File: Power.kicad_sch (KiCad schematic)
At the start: 30 parts, among them J1 Jack-DC, J2 USB_B_Micro, J3 MCU_VOLTAGE_SEL, U1 LM2596S-5, U3 LM1117-3.3, U4 LM1117-1.8, U5 TPS2552DBVR

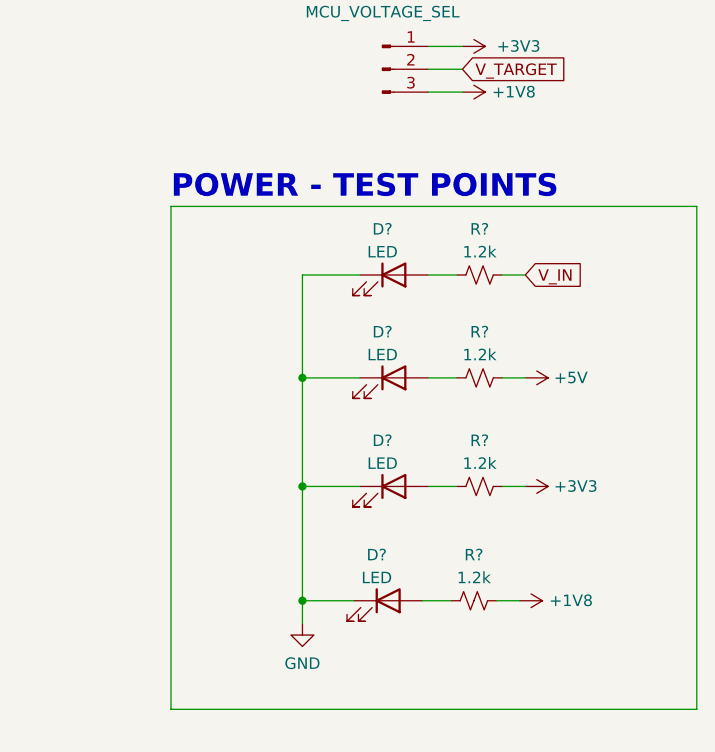
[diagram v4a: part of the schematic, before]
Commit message: Power ledler eklendi
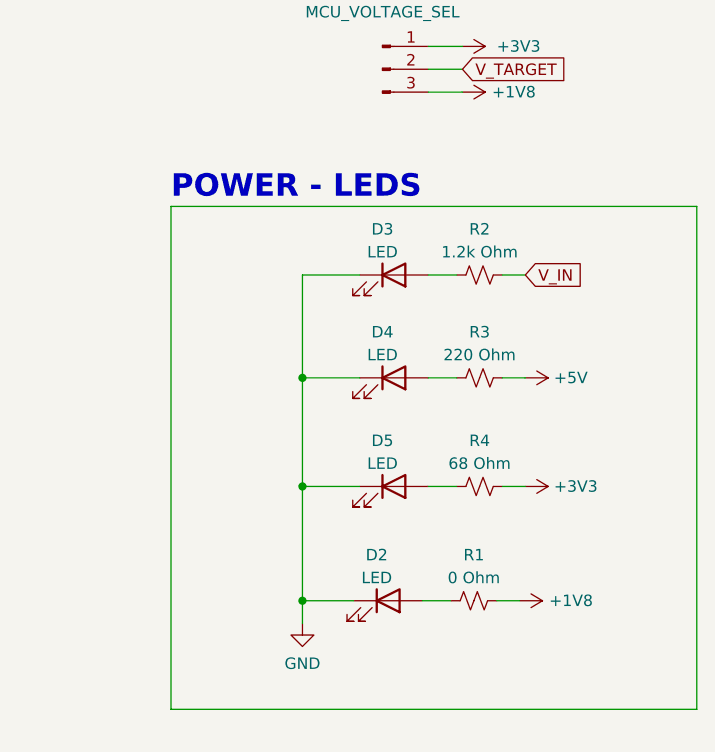
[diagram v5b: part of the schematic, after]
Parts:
- D2, D3, D4, D5: renamed from D?; footprint (none) -> LED_SMD:LED_0805_2012Metric
- R1: renamed from R?; value 1.2k -> 0 Ohm; footprint (none) -> Resistor_SMD:R_0603_1608Metric
- R2: renamed from R?; value 1.2k -> 1.2k Ohm; footprint (none) -> Resistor_SMD:R_0603_1608Metric
- R3: renamed from R?; value 1.2k -> 220 Ohm; footprint (none) -> Resistor_SMD:R_0603_1608Metric
- R4: renamed from R?; value 1.2k -> 68 Ohm; footprint (none) -> Resistor_SMD:R_0603_1608Metric
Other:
- note added: "POWER - LEDS"
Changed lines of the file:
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@@
     (effects (font (size 2.5 2.5) (thickness 0.5) bold) (justify left bottom))
   )
-  (text "POWER - TEST POINTS" (at 222.25 106.045 0)
+  (text "POWER - LEDS" (at 222.25 106.045 0)
     (effects (font (size 2.5 2.5) (thickness 0.5) bold) (justify left bottom))
   )
@@
   (symbol (lib_id "Device:R_Small_US") (at 255.905 150.495 90) (unit 1)
     (in_bom yes) (on_board yes)
-    (property "Reference" "R?" (id 0) (at 255.905 145.415 90))
-    (property "Value" "1.2k" (id 1) (at 255.905 147.955 90))
-    (property "Footprint" "" (id 2) (at 255.905 150.495 0)
+    (property "Reference" "R1" (id 0) (at 255.905 145.415 90))
+    (property "Value" "0 Ohm" (id 1) (at 255.905 147.955 90))
+    (property "Footprint" "Resistor_SMD:R_0603_1608Metric" (id 2) (at 255.905 150.495 0)
       (effects (font (size 1.27 1.27)) hide)
     )
@@
   (symbol (lib_id "Device:R_Small_US") (at 256.54 125.73 90) (unit 1)
     (in_bom yes) (on_board yes)
-    (property "Reference" "R?" (id 0) (at 256.54 120.65 90))
-    (property "Value" "1.2k" (id 1) (at 256.54 123.19 90))
-    (property "Footprint" "" (id 2) (at 256.54 125.73 0)
+    (property "Reference" "R3" (id 0) (at 256.54 120.65 90))
+    (property "Value" "220 Ohm" (id 1) (at 256.54 123.19 90))
+    (property "Footprint" "Resistor_SMD:R_0603_1608Metric" (id 2) (at 256.54 125.73 0)
       (effects (font (size 1.27 1.27)) hide)
     )
@@
   (symbol (lib_id "power:+1V8") (at 260.985 150.495 270) (unit 1)
     (in_bom yes) (on_board yes)
-    (property "Reference" "#PWR?" (id 0) (at 257.175 150.495 0)
+    (property "Reference" "#PWR0125" (id 0) (at 257.175 150.495 0)
       (effects (font (size 1.27 1.27)) hide)
     )
@@
   (symbol (lib_id "Device:R_Small_US") (at 256.54 137.795 90) (unit 1)
     (in_bom yes) (on_board yes)
-    (property "Reference" "R?" (id 0) (at 256.54 132.715 90))
-    (property "Value" "1.2k" (id 1) (at 256.54 135.255 90))
-    (property "Footprint" "" (id 2) (at 256.54 137.795 0)
+    (property "Reference" "R4" (id 0) (at 256.54 132.715 90))
+    (property "Value" "68 Ohm" (id 1) (at 256.54 135.255 90))
+    (property "Footprint" "Resistor_SMD:R_0603_1608Metric" (id 2) (at 256.54 137.795 0)
       (effects (font (size 1.27 1.27)) hide)
     )
@@
   (symbol (lib_name "LED_1") (lib_id "Device:LED") (at 246.38 150.495 0) (unit 1)
     (in_bom yes) (on_board yes)
-    (property "Reference" "D?" (id 0) (at 245.11 145.415 0))
+    (property "Reference" "D2" (id 0) (at 245.11 145.415 0))
     (property "Value" "LED" (id 1) (at 245.11 147.955 0))
-    (property "Footprint" "" (id 2) (at 246.38 150.495 0)
+    (property "Footprint" "LED_SMD:LED_0805_2012Metric" (id 2) (at 246.38 150.495 0)
       (effects (font (size 1.27 1.27)) hide)
     )
@@
   (symbol (lib_id "power:+3V3") (at 261.62 137.795 270) (unit 1)
     (in_bom yes) (on_board yes) (fields_autoplaced)
-    (property "Reference" "#PWR?" (id 0) (at 257.81 137.795 0)
+    (property "Reference" "#PWR0123" (id 0) (at 257.81 137.795 0)
       (effects (font (size 1.27 1.27)) hide)
     )
@@
   (symbol (lib_id "Device:R_Small_US") (at 256.54 114.3 90) (unit 1)
     (in_bom yes) (on_board yes)
-    (property "Reference" "R?" (id 0) (at 256.54 109.22 90))
-    (property "Value" "1.2k" (id 1) (at 256.54 111.76 90))
-    (property "Footprint" "" (id 2) (at 256.54 114.3 0)
+    (property "Reference" "R2" (id 0) (at 256.54 109.22 90))
+    (property "Value" "1.2k Ohm" (id 1) (at 256.54 111.76 90))
+    (property "Footprint" "Resistor_SMD:R_0603_1608Metric" (id 2) (at 256.54 114.3 0)
       (effects (font (size 1.27 1.27)) hide)
     )
@@
   (symbol (lib_name "LED_1") (lib_id "Device:LED") (at 247.015 125.73 0) (unit 1)
     (in_bom yes) (on_board yes)
-    (property "Reference" "D?" (id 0) (at 245.745 120.65 0))
+    (property "Reference" "D4" (id 0) (at 245.745 120.65 0))
     (property "Value" "LED" (id 1) (at 245.745 123.19 0))
-    (property "Footprint" "" (id 2) (at 247.015 125.73 0)
+    (property "Footprint" "LED_SMD:LED_0805_2012Metric" (id 2) (at 247.015 125.73 0)
       (effects (font (size 1.27 1.27)) hide)
     )
@@
   (symbol (lib_name "LED_1") (lib_id "Device:LED") (at 247.015 137.795 0) (unit 1)
     (in_bom yes) (on_board yes)
-    (property "Reference" "D?" (id 0) (at 245.745 132.715 0))
+    (property "Reference" "D5" (id 0) (at 245.745 132.715 0))
     (property "Value" "LED" (id 1) (at 245.745 135.255 0))
-    (property "Footprint" "" (id 2) (at 247.015 137.795 0)
+    (property "Footprint" "LED_SMD:LED_0805_2012Metric" (id 2) (at 247.015 137.795 0)
       (effects (font (size 1.27 1.27)) hide)
     )
@@
   (symbol (lib_id "power:GND") (at 236.855 153.035 0) (mirror y) (unit 1)
     (in_bom yes) (on_board yes) (fields_autoplaced)
-    (property "Reference" "#PWR?" (id 0) (at 236.855 159.385 0)
+    (property "Reference" "#PWR0122" (id 0) (at 236.855 159.385 0)
       (effects (font (size 1.27 1.27)) hide)
     )
@@
   (symbol (lib_id "power:+5V") (at 261.62 125.73 270) (unit 1)
     (in_bom yes) (on_board yes) (fields_autoplaced)
-    (property "Reference" "#PWR?" (id 0) (at 257.81 125.73 0)
+    (property "Reference" "#PWR0124" (id 0) (at 257.81 125.73 0)
       (effects (font (size 1.27 1.27)) hide)
     )
@@
   (symbol (lib_name "LED_1") (lib_id "Device:LED") (at 247.015 114.3 0) (unit 1)
     (in_bom yes) (on_board yes)
-    (property "Reference" "D?" (id 0) (at 245.745 109.22 0))
+    (property "Reference" "D3" (id 0) (at 245.745 109.22 0))
     (property "Value" "LED" (id 1) (at 245.745 111.76 0))
-    (property "Footprint" "" (id 2) (at 247.015 114.3 0)
-      (effects (font (size 1.27 1.27)) hide)
-    )
+    (property "Footprint" "LED_SMD:LED_0805_2012Metric" (id 2) (at 247.015 114.3 0)
+      (effects (font (size 1.27 1.27)) hide)
+    )

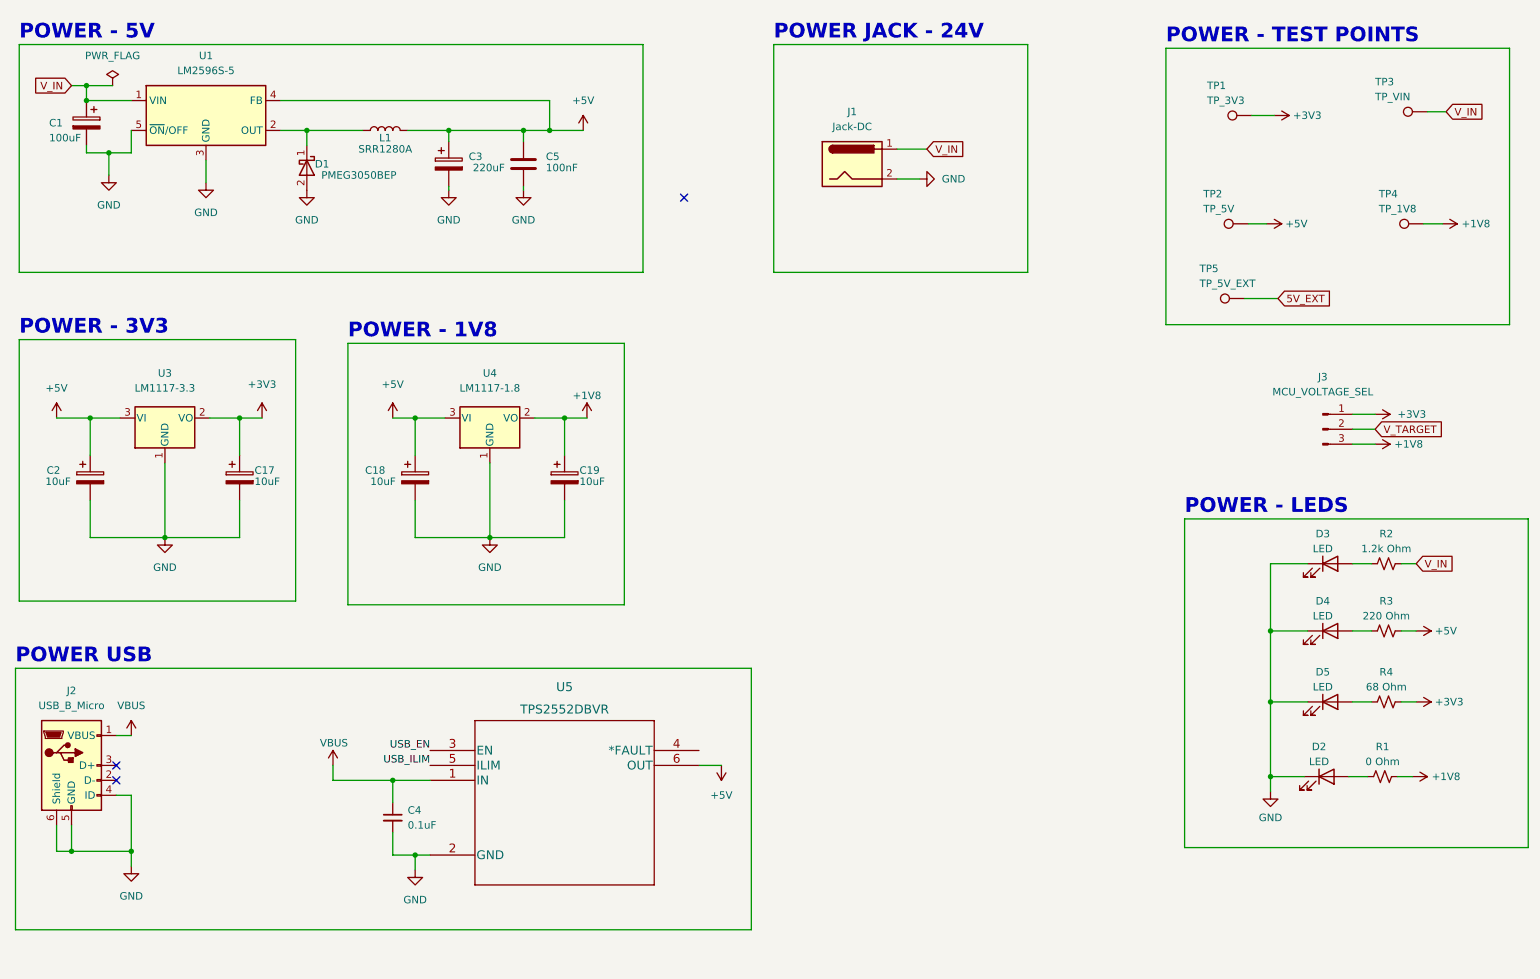
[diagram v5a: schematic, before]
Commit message: USB Current limiting devresi tamamlanacak. ADC bağlantıları yapılıyor
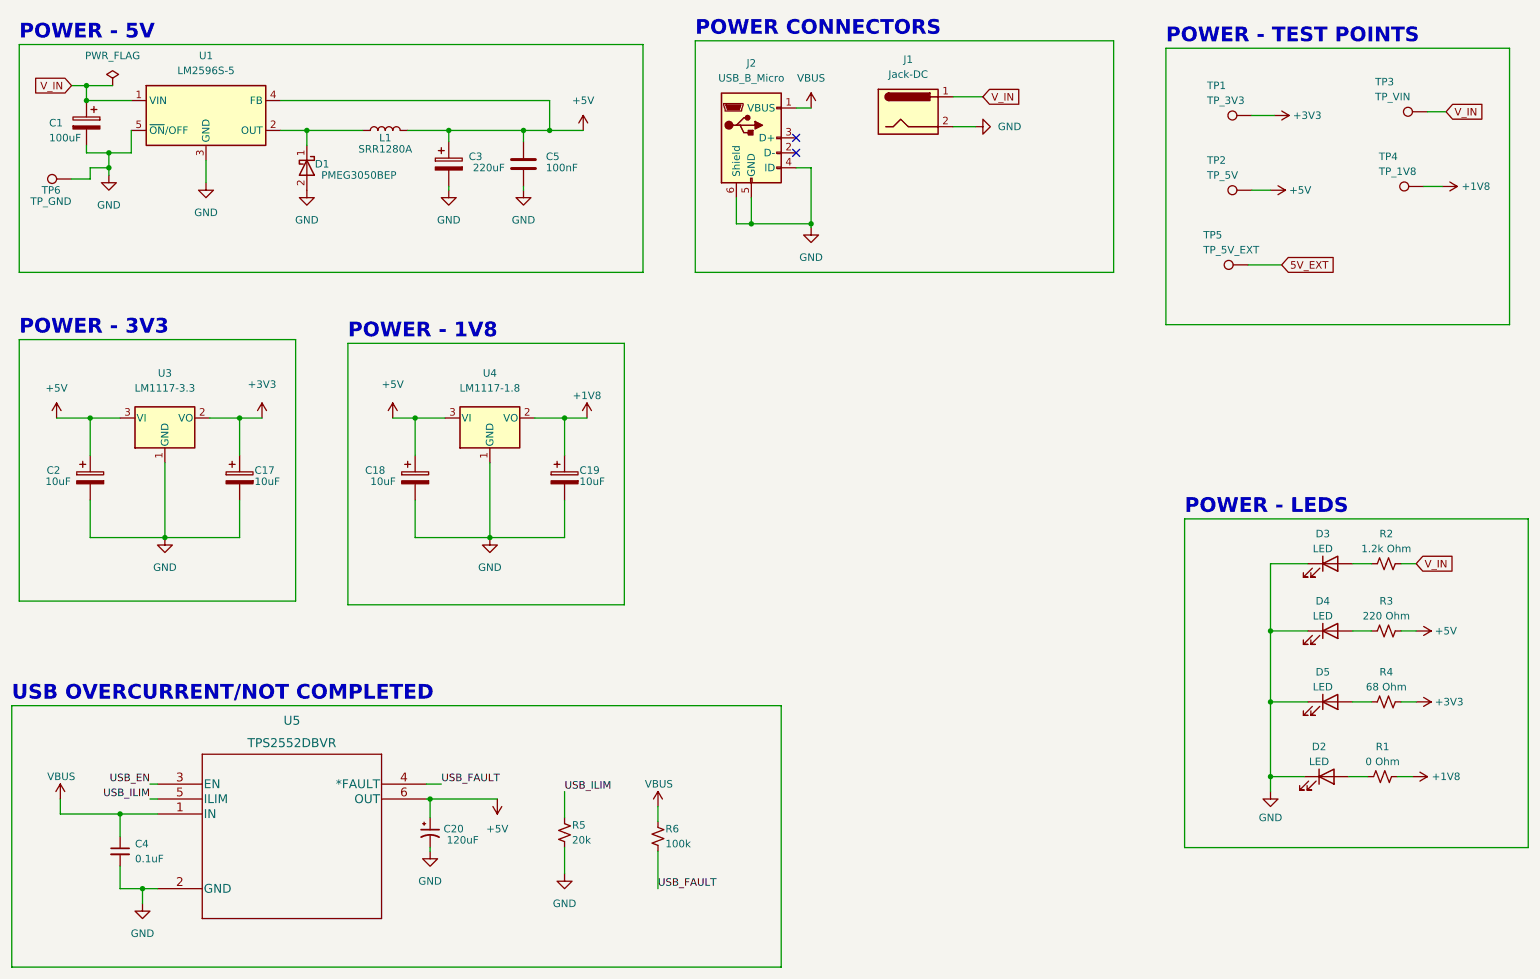
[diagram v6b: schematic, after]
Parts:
- removed J3: MCU_VOLTAGE_SEL, Connector_PinHeader_2.54mm:PinHeader_1x03_P2.54mm_Vertical, symbol Connector:Conn_01x03_Male
- added C20: 120uF, symbol Device:C_Polarized_Small_US
- added R5: 20k, Resistor_SMD:R_0603_1608Metric, symbol Device:R_Small_US
- added R6: 100k, Resistor_SMD:R_0603_1608Metric, symbol Device:R_Small_US
- added TP6: TP_GND, TestPoint:TestPoint_Pad_D1.0mm, symbol Connector:TestPoint
- C4: footprint (none) -> Capacitor_SMD:C_0603_1608Metric
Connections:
- net +5V: now also C20.1
- net GND: now also C20.2, R5.2, TP6.1
- net USB_ILIM: now also R5.1
- net VBUS: now also R6.1
- net USB_FAULT: now reaches U5.4 (*FAULT)
- net USB_FAULT: now also R6.2
- no-connect marks 3 -> 2
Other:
- note added: "POWER CONNECTORS"
- note added: "USB OVERCURRENT/NOT COMPLETED"
- note removed: "POWER JACK - 24V"
- note removed: "POWER USB"
- moved on the sheet: J2, TP2, TP4, TP5

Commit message: Reset devresi eklenecek.
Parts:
- U5: footprint erkan-hw-lib:TPS2552DBVR -> erkan-hw-lib:HPA00714DBVR
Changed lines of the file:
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@@
     (pin "1")
   )
-  (symbol (lib_name "LED_1") (lib_id "Device:LED") (at 246.38 150.495 0) (unit 1)
+  (symbol (lib_id "Device:LED") (at 246.38 150.495 0) (unit 1)
     (in_bom yes) (on_board yes)
     (property "Reference" "D2" (id 0) (at 245.11 145.415 0))
@@
       (effects (font (size 1.524 1.524)))
     )
-    (property "Footprint" "erkan-hw-lib:TPS2552DBVR" (id 2) (at 70.485 145.669 0)
+    (property "Footprint" "erkan-hw-lib:HPA00714DBVR" (id 2) (at 70.485 145.669 0)
       (effects (font (size 1.524 1.524)) hide)
     )
@@
     (pin "1")
   )
-  (symbol (lib_name "LED_1") (lib_id "Device:LED") (at 247.015 125.73 0) (unit 1)
+  (symbol (lib_id "Device:LED") (at 247.015 125.73 0) (unit 1)
     (in_bom yes) (on_board yes)
     (property "Reference" "D4" (id 0) (at 245.745 120.65 0))
@@
     (pin "3")
   )
-  (symbol (lib_name "LED_1") (lib_id "Device:LED") (at 247.015 137.795 0) (unit 1)
+  (symbol (lib_id "Device:LED") (at 247.015 137.795 0) (unit 1)
     (in_bom yes) (on_board yes)
     (property "Reference" "D5" (id 0) (at 245.745 132.715 0))
@@
     (pin "1")
   )
-  (symbol (lib_name "LED_1") (lib_id "Device:LED") (at 247.015 114.3 0) (unit 1)
+  (symbol (lib_id "Device:LED") (at 247.015 114.3 0) (unit 1)
     (in_bom yes) (on_board yes)
     (property "Reference" "D3" (id 0) (at 245.745 109.22 0))
